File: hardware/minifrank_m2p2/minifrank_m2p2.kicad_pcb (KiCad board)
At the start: 4 copper layers, 85.6 x 54 mm, 136 parts, among them J1 PWR, J10 VGA, J11 PJ-320D, J12 104031-0811, J2 UART, J3 DEBUG, J4 SS-52100-004, J5 USB4215-03-A, J6 MDC-036, J7 PJ-320D, J8 DC3RX19JA2, J9 GP2, U1 TS3USB221RSER, U10 ESP-01v090, U11 TDA1387T, U12 LM358, U2 USBLC6-2SC6, U3 MW7211A, U4 NCP1117-3.3_SOT223, U5 TXS0104ERGYR, U6 ESP-PSRAM32, U7 W25Q128JVS, U8 CD4069UBM, U9 RP2350, Y1 ASE-12MHz

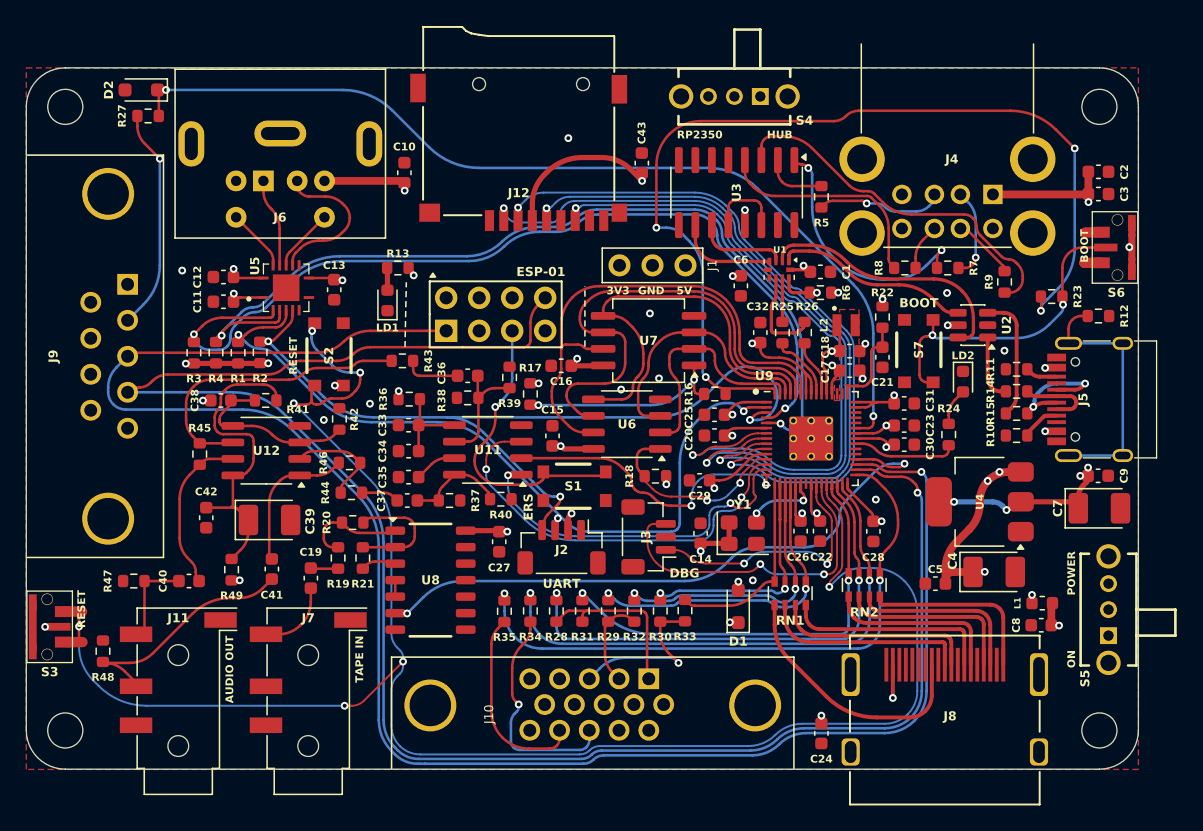
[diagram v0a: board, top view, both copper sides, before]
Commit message: Move lab/ to frank-lab repo, restore minifrank_m2p2 v1.04 from master
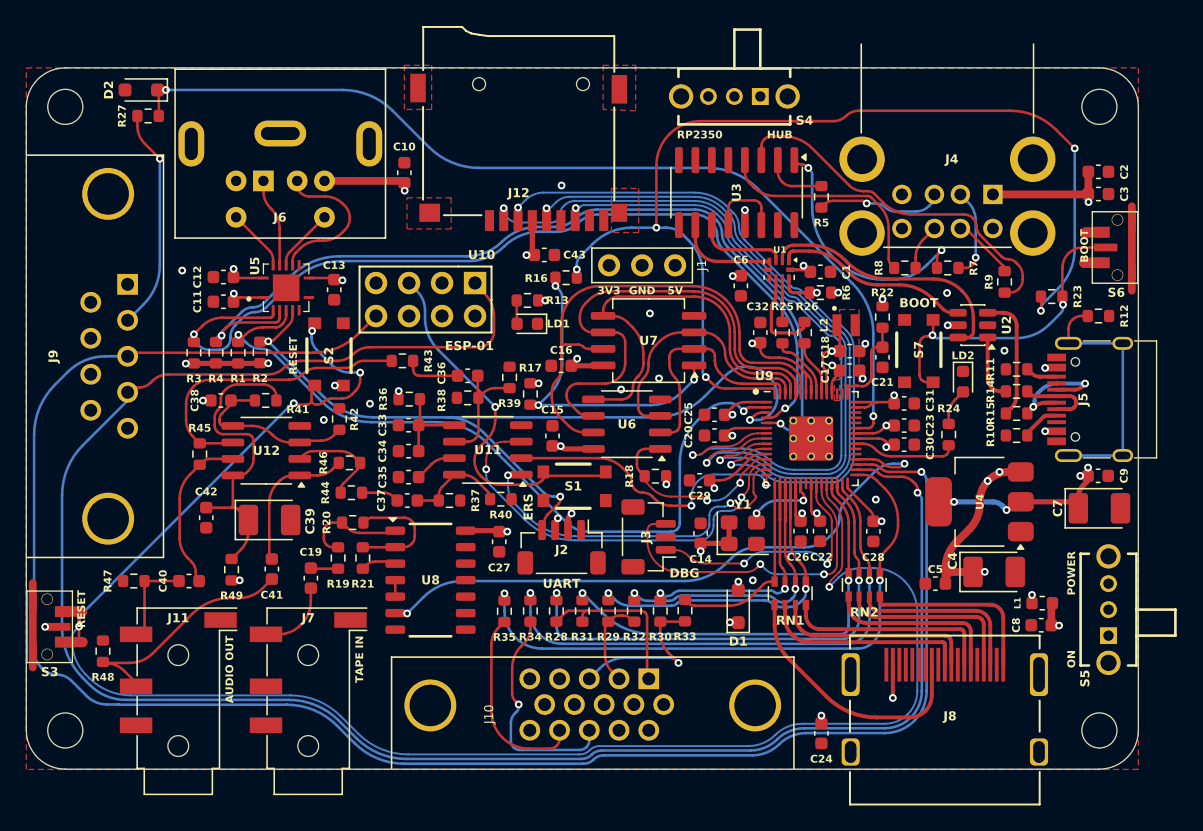
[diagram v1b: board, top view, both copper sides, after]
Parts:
- moved R16 14.5 mm to (172.2, 80.0)
- moved LD1 10.9 mm to (169.3, 83.5), turned to 180 degrees
- moved C43 10.3 mm to (170.6, 78.2), turned to 180 degrees
- moved R13 10.3 mm to (169.3, 81.7)
- moved U10 4.30 mm to (165.2, 80.4), turned to -90 degrees
- moved J1 0.80 mm to (175.6, 79.0)
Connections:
- U10 pad 1: /GPIO21 -> /GPIO20
- U10 pad 8: /GPIO20 -> /GPIO21
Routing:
- net +3V3: track 79.9 -> 69.6 mm
- net /RP2350A/FLASH_SS: track 15.5 -> 23.7 mm, vias 2 -> 3
- net /RP2350A/QSPI_SS: track 73.9 -> 81.5 mm, vias 4 -> 5
- net /GPIO21: track 136.8 -> 143.4 mm
- net /GPIO20: track 140.6 -> 146.7 mm
- net /RUN: track 145.9 -> 139.9 mm, vias 7 -> 5
- net GND: track 10.1 -> 16.1 mm, vias 17 -> 16
- net /ESP_RST: track 22.0 -> 27.7 mm

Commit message: Board updates
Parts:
- moved R16 14.5 mm to (183.7, 88.9)
- moved LD1 10.9 mm to (158.5, 81.7), turned to 90 degrees
- moved C43 10.3 mm to (178.1, 71.1), turned to -90 degrees
- moved R13 10.3 mm to (159.3, 79.2)
- moved U10 4.30 mm to (163.0, 84.0), turned to 90 degrees
- moved J1 0.80 mm to (176.4, 79.0)
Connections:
- U10 pad 1: /GPIO20 -> /GPIO21
- U10 pad 8: /GPIO21 -> /GPIO20
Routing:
- net +3V3: track 69.6 -> 79.9 mm
- net /RP2350A/FLASH_SS: track 23.7 -> 15.5 mm, vias 3 -> 2
- net /RP2350A/QSPI_SS: track 81.5 -> 73.9 mm, vias 5 -> 4
- net /GPIO21: track 143.4 -> 136.8 mm
- net /GPIO20: track 146.7 -> 140.6 mm
- net /RUN: track 139.9 -> 145.9 mm, vias 5 -> 7
- net GND: track 16.1 -> 10.1 mm, vias 16 -> 17
- net /ESP_RST: track 27.7 -> 22.0 mm
